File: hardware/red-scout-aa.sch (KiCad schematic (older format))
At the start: 41 parts, among them P1 SNAP, P1.1 PIN, P2 SNAP, P2.1 PIN, P3 SNAP, P3.1 PIN, P4 SNAP, P4.1 PIN, P5 SNAP, P5.1 PIN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

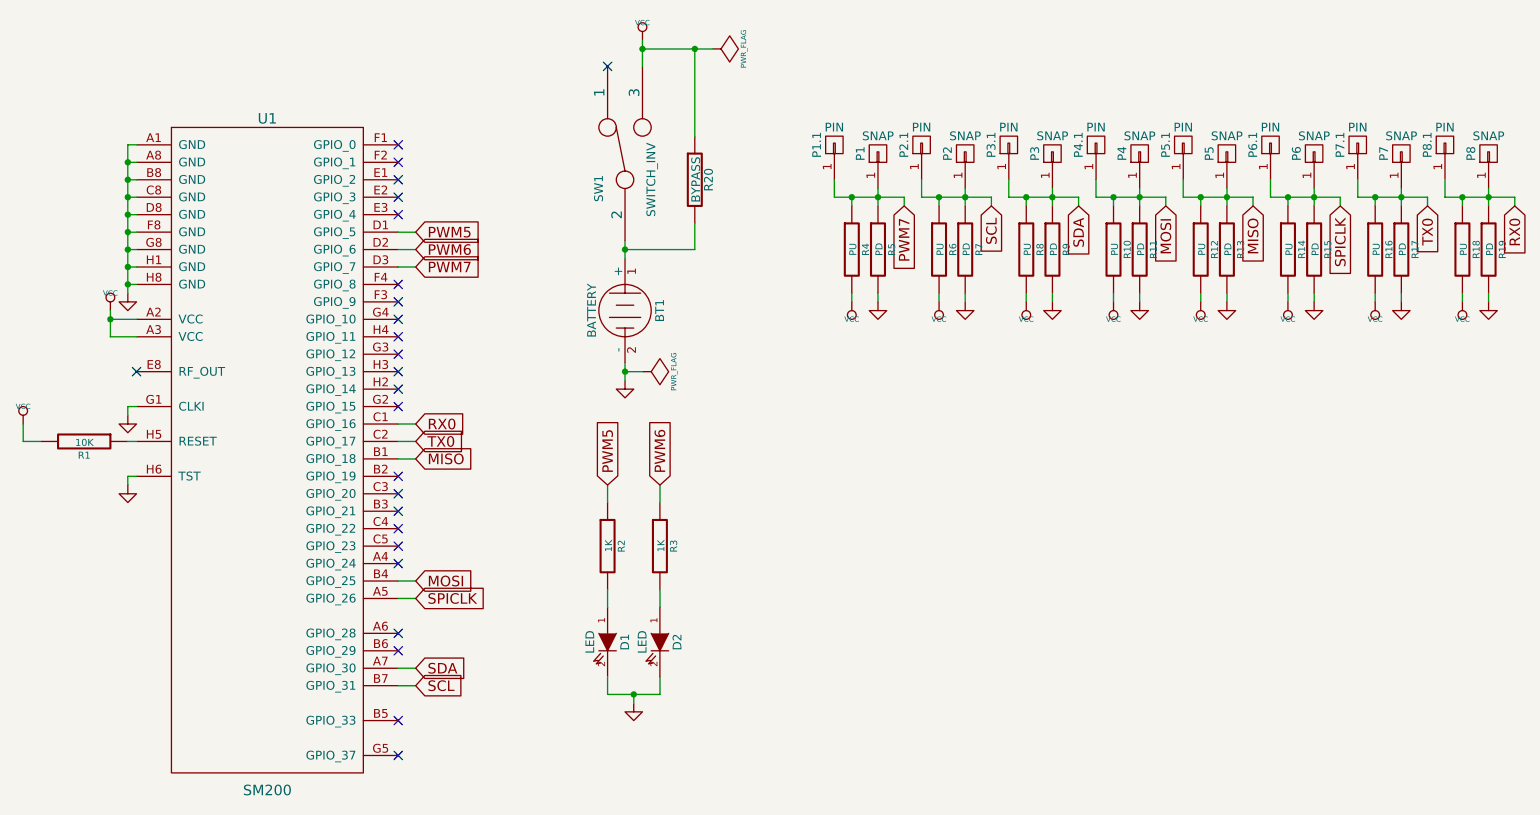
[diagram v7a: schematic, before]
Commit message: Add serial port and fix IO header.
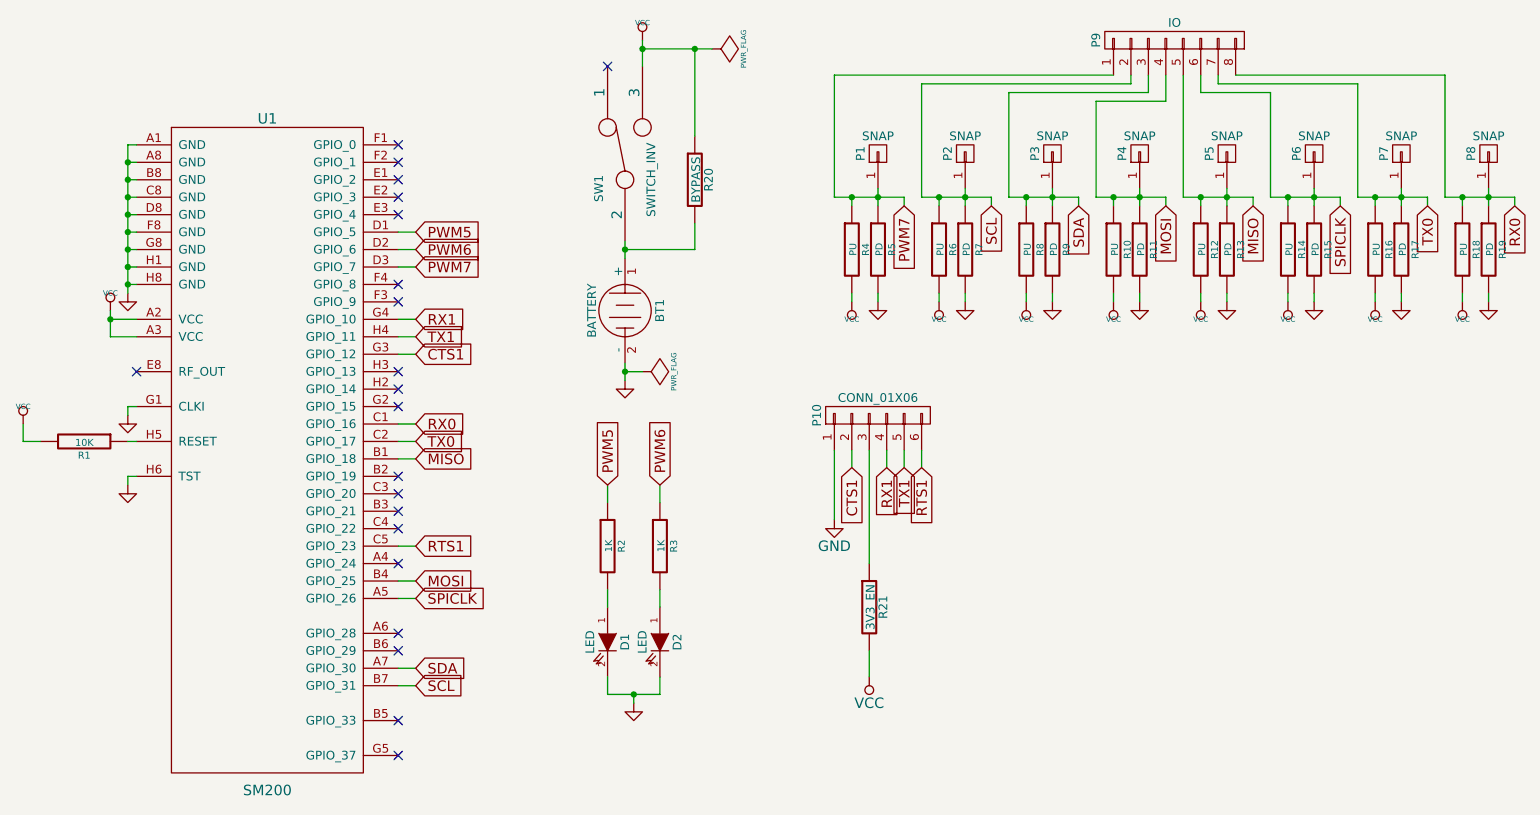
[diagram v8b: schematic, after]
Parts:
- removed P1.1, P2.1, P3.1, P4.1, P5.1, P6.1, P7.1, P8.1: PIN, _CrumpPrints:16_snap, symbol CONN_01X01
- added P10: CONN_01X06, symbol CONN_01X06
- added P9: IO, symbol CONN_01X08
- added R21: 3V3_EN, symbol R
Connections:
- net GND: now also P10.1 (P1)
- net MISO: now also P9.5 (P5)
- net MOSI: now also P9.4 (P4)
- net PWM7: now also P9.1 (P1)
- net RX0: now also P9.8 (P8)
- net SCL: now also P9.2 (P2)
- net SDA: now also P9.3 (P3)
- net SPICLK: now also P9.6 (P6)
- net TX0: now also P9.7 (P7)
- net VCC: now also R21.2
- net RTS1: now reaches U1.C5 (GPIO_23)
- net RTS1: now also P10.6 (P6)
- net CTS1: now reaches U1.G3 (GPIO_12)
- net CTS1: now also P10.2 (P2)
- net RX1: now reaches U1.G4 (GPIO_10)
- net RX1: now also P10.4 (P4)
- net TX1: now reaches U1.H4 (GPIO_11)
- net TX1: now also P10.5 (P5)
- new net: P10.3 (P3), R21.1
- no-connect marks 25 -> 21
